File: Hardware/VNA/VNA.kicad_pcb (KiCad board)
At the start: 4 copper layers, 100 x 67 mm, 244 parts, among them J1 USB_B_Micro, J2 USB_A, J3 Conn_ARM_SWD, J4 SMA, J5 SMA, J6 UART, Q1 RE1C002UN, SW1 SW_Push, SW2 SW_Push, SW3 SW_Push, U1 TPD2S017, U10 74AHC1G04, U11 PE42440, U12 SN74LVC1G139, U13 PE42440, U14 F2923, U15 AD8302, U16 STM32F373RCTx, U17 AT25SF081-SSHD-X, U2 TPD2S017, U3 MAX2871, U4 LP5912, U5 LP5912, U6 MIC5366-1.8, U7 AD8319, U8 SKY12347-362LF, U9 TRF37A75, X1 ASTXR-12-19.200MHz, Y1 8MHz

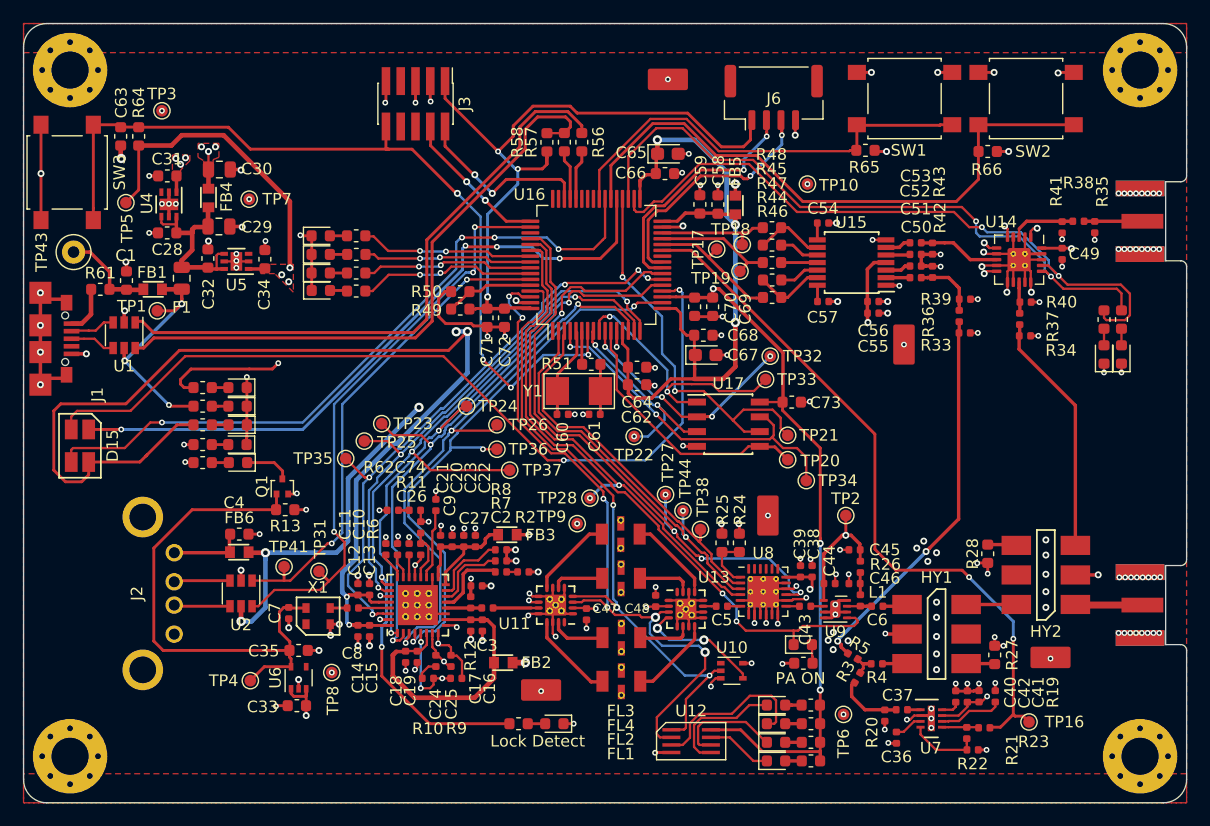
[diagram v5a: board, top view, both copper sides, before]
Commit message: Layout done, front and rear panels designed
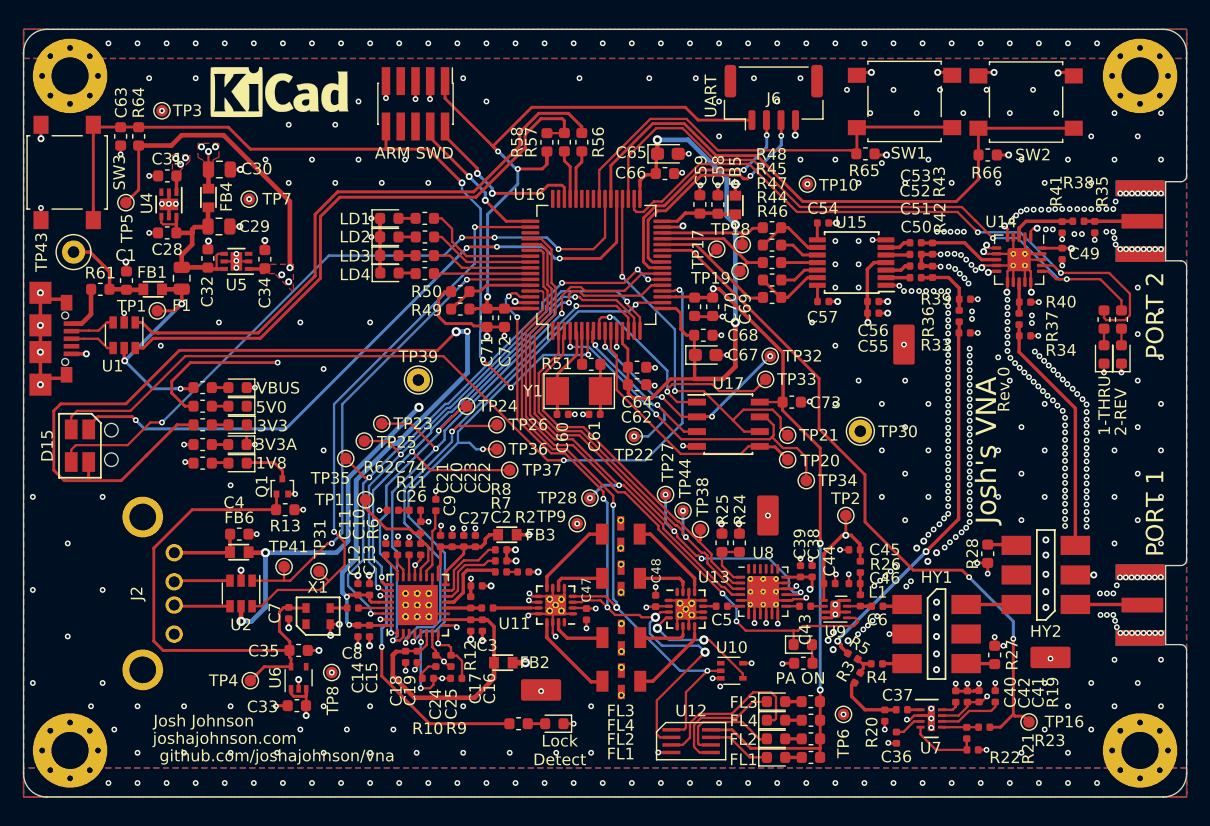
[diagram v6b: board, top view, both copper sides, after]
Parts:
- added G***: LOGO, VNA_Footprints:OSHW_Logo_3.6x3.6_F.Mask, F.Cu at (176.0, 98.2)
- added REF**: KiCAD Logo, Symbol:Symbol_KiCAD-Logo_CopperAndSilkScreenTop, F.Cu at (112.2, 67.0)
- added REF**: Josh Details, VNA_Footprints:JoshDetails, F.Cu at (105.5, 122.8)
- added REF**: Board Title, VNA_Footprints:BoardTitle, F.Cu at (137.5, 63.0)
- added TP30: GND, TestPoint:TestPoint_THTPad_D2.0mm_Drill1.0mm, F.Cu at (162.2, 96.3)
- added TP39: GND, TestPoint:TestPoint_THTPad_D2.0mm_Drill1.0mm, F.Cu at (124.2, 92.0)
- added TP40: Light Pipe, VNA_Footprints:SLP3-150-150-F, F.Cu at (100.2, 98.8)
- TP11: value GND -> CP; footprint VNA_Footprints:S1751-46_smdTestPoint -> TestPoint:TestPoint_Pad_D1.0mm
- moved TP11 44.5 mm to (119.6, 102.2)
- moved D11 6.09 mm to (121.7, 78.0)
- moved D12 6.09 mm to (121.7, 79.7)
- moved D13 6.09 mm to (121.7, 81.2)
- moved R52 6.09 mm to (124.7, 78.0)
- moved R53 6.09 mm to (124.7, 79.7)
- moved R54 6.09 mm to (124.7, 81.2)
- moved R55 6.09 mm to (124.7, 82.8)
- moved D14 6.09 mm to (121.7, 82.8)
- moved D5 1.60 mm to (108.6, 94.2)
- moved D6 1.60 mm to (108.6, 92.6)
- moved R17 1.60 mm to (105.6, 94.2)
- moved R18 1.60 mm to (105.6, 92.6)
- moved H1 0.50 mm to (94.2, 65.8)
- moved H2 0.50 mm to (186.2, 123.8)
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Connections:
- TP11 pad 1: GND -> Net-(C26-Pad1)
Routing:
- net GND: track 225.2 -> 211.0 mm, vias 209 -> 631
- net Net-(R55-Pad2): track 15.4 -> 8.28 mm, vias 2 -> 0
- net Net-(C26-Pad1): track 4.73 -> 11.1 mm
- net Net-(R54-Pad2): track 14.8 -> 9.17 mm, vias 2 -> 0
- net Net-(R53-Pad2): track 14.5 -> 9.17 mm, vias 2 -> 0
- net Net-(R52-Pad2): track 14.9 -> 10.3 mm, vias 2 -> 0
- net VDD: track 250.0 -> 246.8 mm
- net /5V0: track 133.3 -> 135.8 mm
- net /USB_D+: track 53.5 -> 51.5 mm
- net /USB_D-: track 52.7 -> 51.3 mm
- net /Microcontroller/STATUS_LED_B: track 60.4 -> 59.0 mm
- net /RF_PWR_LEVEL: track 61.3 -> 60.4 mm
- net /SWD_IO: track 15.7 -> 15.0 mm
- net /SWD_nRST: track 72.7 -> 73.4 mm
- net /VBUS: track 20.8 -> 20.3 mm
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- added copper zone on B.Cu, net GND
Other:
- board size 100 x 67 mm -> 100 x 66 mm
- board text added: "1-THRU"
- board text added: "1V8"
- board text added: "2-REV"
- board text added: "3V3"
- board text added: "3V3A"
- board text added: "5V0"
- board text added: "ARM SWD"
- board text added: "FL1"
- board text added: "FL2"
- board text added: "FL3"
- board text added: "FL4"
- board text added: "LD1"
- board text added: "LD2"
- board text added: "LD3"
- board text added: "LD4"
- board text added: "PORT 1"
- board text added: "PORT 2"
- board text added: "UART"
- board text added: "VBUS"

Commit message: Gerbers generated, ready for fab
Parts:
- added TP29: Test2, TestPoint:TestPoint_Pad_D1.0mm, F.Cu at (139.8, 67.1)
- added TP42: Test1, TestPoint:TestPoint_Pad_D1.0mm, F.Cu at (142.3, 67.1)
- added TP45: Test3, TestPoint:TestPoint_Pad_D1.0mm, F.Cu at (137.3, 67.1)
- U12: footprint VNA_Footprints:VSSOP-8_2.9x3.15mm_P0.65 -> Package_SO:VSSOP-8_2.3x2mm_P0.5mm
- moved TP32 2.21 mm to (153.7, 92.0)
- moved TP33 1.94 mm to (154.4, 90.0)
- moved U12 0.36 mm to (147.4, 122.7), turned to 0 degrees
- moved TP22 0.22 mm to (142.9, 96.9)
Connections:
- U16 pad 10: /Microcontroller/FLASH_SPI_MISO -> /MAX2871_MISO
- U16 pad 11: /Microcontroller/FLASH_SPI_MOSI -> /MAX2871_MOSI
- U16 pad 14: /MAX2871_LE -> /MAX2871_LD
- U16 pad 15: /MAX2871_LD -> /MAX2871_RFOUT_EN
- U16 pad 16: /MAX2871_RFOUT_EN -> /Microcontroller/FLASH_nCS
- U16 pad 18: /MAX2871_CHIP_EN -> /Microcontroller/FLASH_nHOLD
- U16 pad 21: /MAX2871_CLK -> /Microcontroller/FLASH_SPI_SCK
- U16 pad 22: /MAX2871_MISO -> /Microcontroller/FLASH_SPI_MISO
- U16 pad 23: /MAX2871_MOSI -> /Microcontroller/FLASH_SPI_MOSI
- U16 pad 36: /Microcontroller/FLASH_SPI_SCK -> /MAX2871_CLK
- U16 pad 4: /Microcontroller/FLASH_nHOLD -> /MAX2871_CHIP_EN
- U16 pad 41: (no net) -> Net-(TP42-Pad1)
- U16 pad 42: (no net) -> Net-(TP29-Pad1)
- U16 pad 43: (no net) -> Net-(TP45-Pad1)
- U16 pad 8: /Microcontroller/FLASH_nWP -> /MAX2871_LE
- U16 pad 9: /Microcontroller/FLASH_nCS -> /Microcontroller/FLASH_nWP
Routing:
- net /Microcontroller/FLASH_SPI_SCK: track 33.7 -> 22.1 mm, vias 2 -> 0
- net Net-(TP45-Pad1): track 0.00 -> 10.7 mm
- net Net-(TP42-Pad1): track 0.00 -> 10.7 mm
- net Net-(TP29-Pad1): track 0.00 -> 10.1 mm
- net /MAX2871_CHIP_EN: track 49.4 -> 42.0 mm
- net /Microcontroller/FLASH_nCS: track 23.0 -> 17.1 mm, vias 2 -> 4
- net /Microcontroller/FLASH_nHOLD: track 30.3 -> 24.9 mm, vias 2 -> 0
- net /MAX2871_MOSI: track 52.6 -> 47.7 mm
- net /MAX2871_LE: track 49.5 -> 46.3 mm
- net /MAX2871_MISO: track 51.0 -> 47.8 mm, vias 5 -> 3
- net /MAX2871_CLK: track 49.0 -> 52.1 mm
- net /Microcontroller/FLASH_SPI_MOSI: track 23.0 -> 26.0 mm
- net /Microcontroller/FLASH_nWP: track 18.0 -> 16.2 mm, vias 3 -> 0
- net /Microcontroller/FLASH_SPI_MISO: track 20.5 -> 22.3 mm, vias 4 -> 2
- net /Microcontroller/STATUS_LED_G: track 73.9 -> 72.2 mm
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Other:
- rule trace_min: 0.15 -> 0
